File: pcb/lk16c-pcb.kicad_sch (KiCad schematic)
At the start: 46 parts, among them J1 Conn_01x04, J2 Conn_01x04, J3 Conn_01x04, J4 Conn_01x04, J5 Conn_01x04, J6 Conn_01x04, J7 PINHD_1x03_ARGB, J8 PINHD_1x05_I2C, SW1 SW_Push, SW10 SW_Push, SW11 SW_Push, SW12 SW_Push, SW13 SW_Push, SW14 SW_Push, SW15 SW_Push, SW16 SW_Push, SW17 SW_Push, SW2 SW_Push, SW3 SW_Push, SW4 SW_Push, SW5 SW_Push, SW6 SW_Push, SW7 SW_Push, SW8 SW_Push, SW9 SW_Push, U1 RaspberryPi_Pico

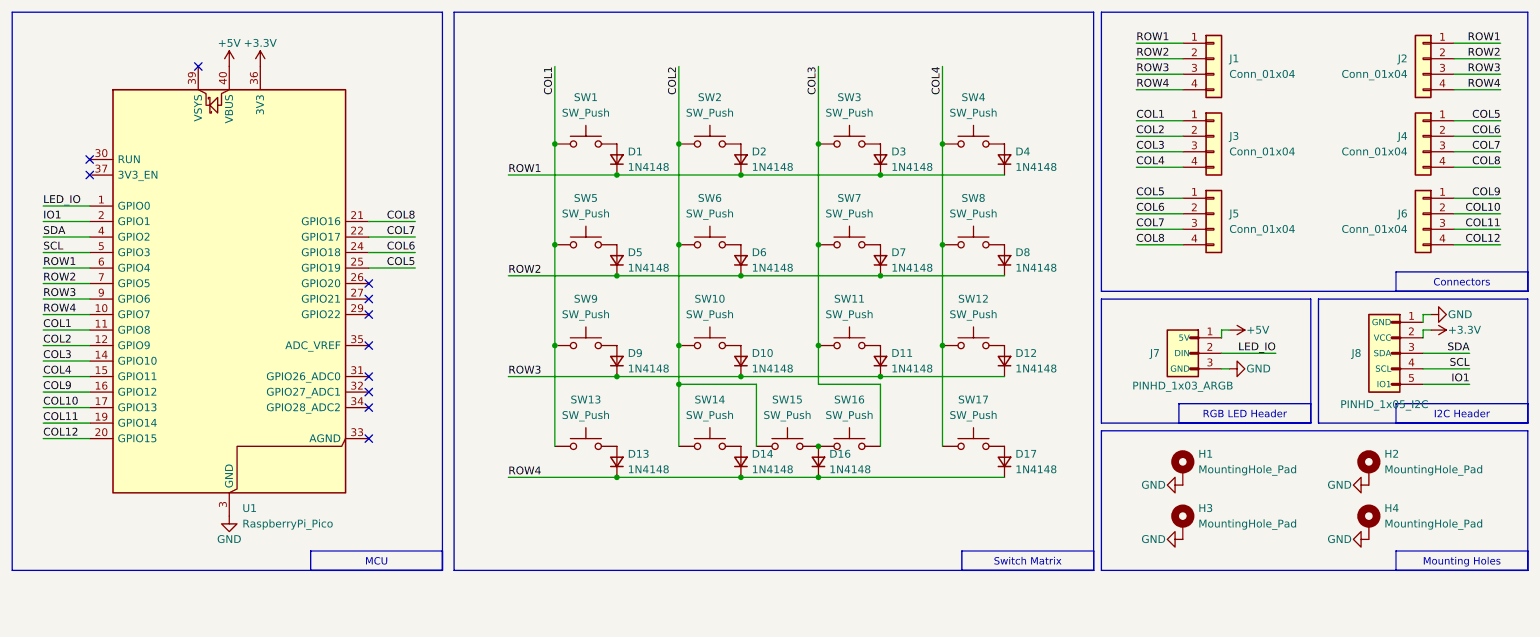
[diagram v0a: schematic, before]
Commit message: Add ability to use 2× 2U Spacebars as the bottom row
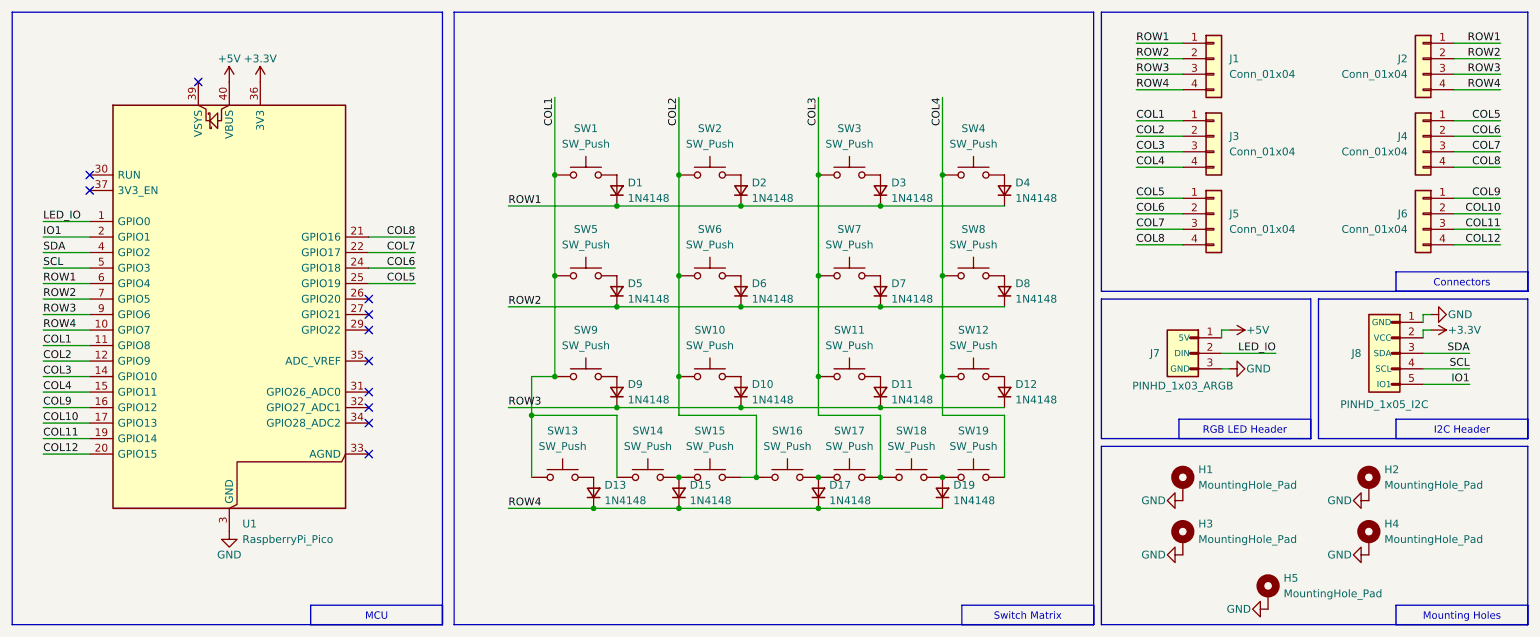
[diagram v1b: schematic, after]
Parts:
- added H5: MountingHole_Pad, LKBD_MountingHole:MountingHole_M2, symbol Mechanical:MountingHole_Pad
- added SW14, SW18: SW_Push, LKBD_KeySwitch:SW_MX_Slim_HotSwap_THT_sqSilk, symbol Switch:SW_Push
- renumbered D14 to D15, D16 to D17, D17 to D19, SW14 to SW15, SW15 to SW16, SW16 to SW17, SW17 to SW19
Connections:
- net COL1: now also SW14.2
- net COL3: now also SW18.2
- net GND: now also H5.1
- net at D15.2 (A), SW15.1: now also SW14.1
- net at D19.2 (A), SW19.1: now also SW18.1
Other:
- moved on the sheet: D1, D10, D11, D12, D13, D15, D17, D19, D2, D3, D4, D5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
